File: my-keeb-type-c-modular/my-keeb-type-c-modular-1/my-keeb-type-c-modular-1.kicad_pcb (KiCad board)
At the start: 2 copper layers, 95.2 x 95.2 mm, 49 parts, among them M1 1x5, M2 1x5

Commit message: Finished type c part 2 and updated type c part 1
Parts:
- moved D23 9.26 mm to (102.4, 112.7), turned to 0 degrees
- moved M2 1.02 mm to (115.8, 106.7), turned to 0 degrees
- moved D20 0.79 mm to (107.2, 55.6)
- moved D21 0.79 mm to (107.2, 74.6)
- moved D22 0.79 mm to (107.2, 93.7)
- moved D19 0.79 mm to (107.2, 36.5)
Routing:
- net ROW4: track 120.2 -> 133.3 mm
- net COL4: track 110.7 -> 100.0 mm
- net COL1: track 147.8 -> 153.8 mm
- net Net-(D23-Pad2): track 6.95 -> 10.4 mm
- net COL0: track 158.8 -> 155.6 mm
- net COL2: track 145.2 -> 143.2 mm
- net COL3: track 122.8 -> 124.6 mm
- net Net-(D22-Pad2): track 11.2 -> 10.4 mm
- net Net-(D21-Pad2): track 11.2 -> 10.4 mm
- net Net-(D20-Pad2): track 11.2 -> 10.4 mm
- net Net-(D19-Pad2): track 11.2 -> 10.4 mm

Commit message: Made sasha smaller
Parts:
- removed the G*** at (49.7, 71.5)
- added G***: LOGO, sasha-small:B.SilkS_layer1, F.Cu at (38.5, 87.6)

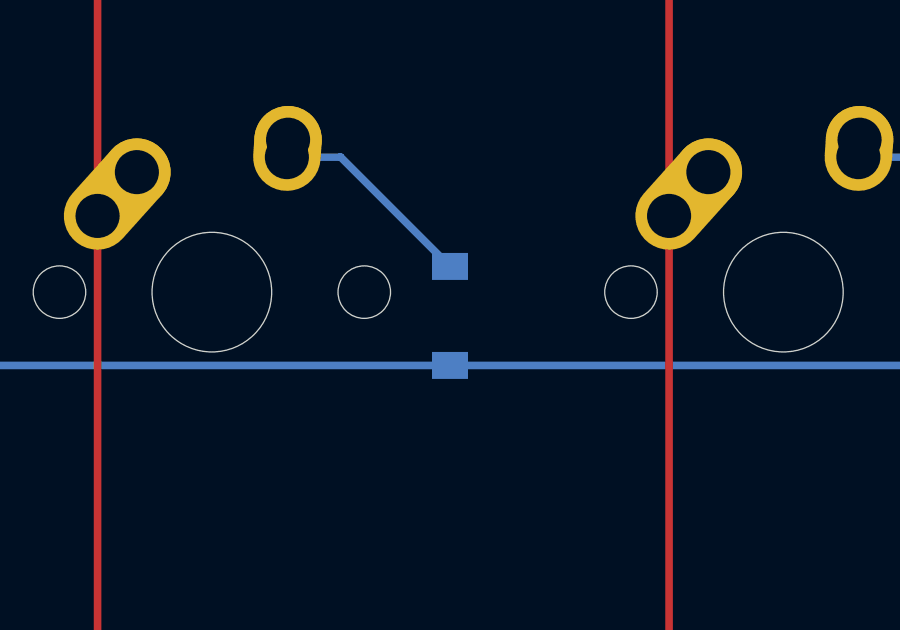
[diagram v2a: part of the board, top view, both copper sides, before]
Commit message: Created some plateless gasket mount pcbs
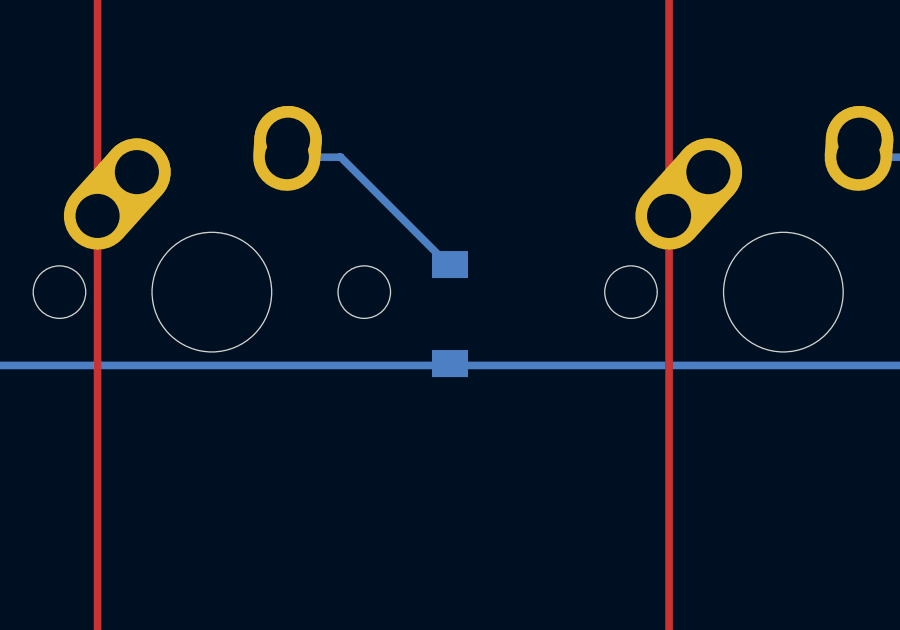
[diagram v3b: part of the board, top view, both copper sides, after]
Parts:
- D1, D10, D11, D12, D13, D14, D15, D16, D17, D18, D19, D2, D20, D21, D22, D23, D3, D4, D5, D6, D7, D8, D9: value SOD-123 -> D_Small
- moved D7 0.06 mm to (57.9, 69.8)
